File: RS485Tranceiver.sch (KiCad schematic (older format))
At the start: 19 parts, among them J8 Conn_01x02, U9 SN75176AD

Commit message: added filters
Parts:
- removed C30, C31: 470p, Capacitor_SMD:C_0603_1608Metric, symbol AR2ISS:C
- removed C32, C33: 1n, Capacitor_SMD:C_0603_1608Metric, symbol AR2ISS:C
- removed D7: PESD2CAN, Package_TO_SOT_SMD:SOT-23_Handsoldering, symbol Device:D_TVS_x2_AAC
- removed J8: Conn_01x02, Connector_PinHeader_2.54mm:PinHeader_1x02_P2.54mm_Vertical, symbol Connector_Generic:Conn_01x02
- removed L3, L4: 10u, Inductor_SMD:L_0603_1608Metric, symbol Device:L
- removed L5, L6: 74279266, Inductor_SMD:L_0603_1608Metric, symbol Device:L
- removed R16, R17: 221, Resistor_SMD:R_0603_1608Metric, symbol AR2ISS:R
- removed R18: 120, Resistor_SMD:R_0603_1608Metric, symbol AR2ISS:R
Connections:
- net sheet60920273/A_Out: now reaches R20.2, R21.1, U9.6 (A)
- net sheet60920273/B_Out: now reaches R19.2, R20.1, U9.7 (B)

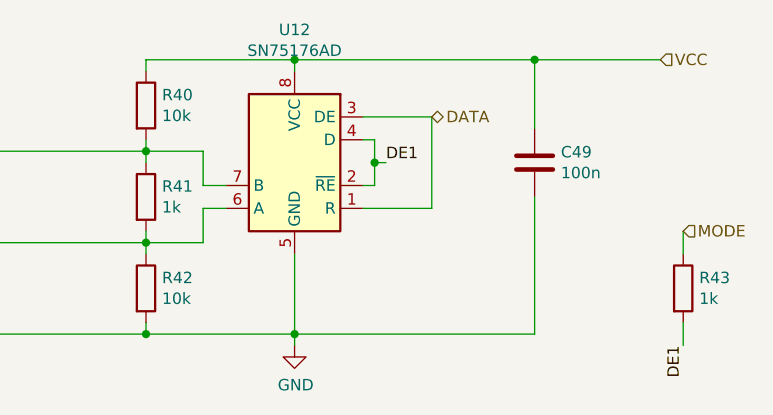
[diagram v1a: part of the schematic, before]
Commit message: updated layout
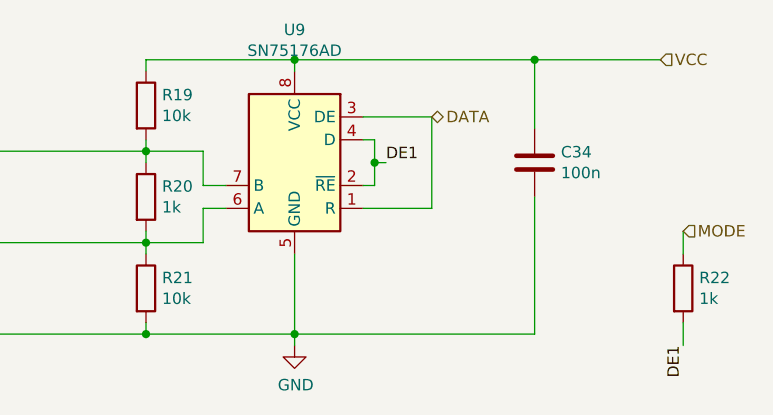
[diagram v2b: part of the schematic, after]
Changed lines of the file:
@@
 $Descr A4 11693 8268
 encoding utf-8
-Sheet 28 31
+Sheet 22 31
 Title ""
 Date ""
@@
 AR Path="/60843FDF/60797D2F/6072BD51" Ref="U10"  Part="1"
 AR Path="/60843FDF/607938CE/6072BD51" Ref="U11"  Part="1"
-F 0 "U12" H 8600 2981 50  0000 C CNN
+F 0 "U9" H 8600 2981 50  0000 C CNN
 F 1 "SN75176AD" H 8600 2890 50  0000 C CNN
 F 2 "Package_SO:SOIC-8_3.9x4.9mm_P1.27mm" H 8600 1900 50  0001 C CNN
@@
 AR Path="/60843FDF/60797D2F/6072BD57" Ref="R28"  Part="1"
 AR Path="/60843FDF/607938CE/6072BD57" Ref="R35"  Part="1"
-F 0 "R42" H 8020 2996 50  0000 L CNN
+F 0 "R21" H 8020 2996 50  0000 L CNN
 F 1 "10k" H 8020 2905 50  0000 L CNN
 F 2 "Resistor_SMD:R_0603_1608Metric" V 7880 2950 50  0001 C CNN
@@
 AR Path="/60843FDF/60797D2F/6072BD5D" Ref="R29"  Part="1"
 AR Path="/60843FDF/607938CE/6072BD5D" Ref="R36"  Part="1"
-F 0 "R43" H 10370 2996 50  0000 L CNN
+F 0 "R22" H 10370 2996 50  0000 L CNN
 F 1 "1k" H 10370 2905 50  0000 L CNN
 F 2 "Resistor_SMD:R_0603_1608Metric" V 10230 2950 50  0001 C CNN
@@
 AR Path="/60843FDF/60797D2F/6072BD63" Ref="R26"  Part="1"
 AR Path="/60843FDF/607938CE/6072BD63" Ref="R33"  Part="1"
-F 0 "R40" H 8020 2196 50  0000 L CNN
+F 0 "R19" H 8020 2196 50  0000 L CNN
 F 1 "10k" H 8020 2105 50  0000 L CNN
 F 2 "Resistor_SMD:R_0603_1608Metric" V 7880 2150 50  0001 C CNN
@@
 AR Path="/60843FDF/60797D2F/6072BD8E" Ref="C39"  Part="1"
 AR Path="/60843FDF/607938CE/6072BD8E" Ref="C44"  Part="1"
-F 0 "C49" H 9765 2446 50  0000 L CNN
+F 0 "C34" H 9765 2446 50  0000 L CNN
 F 1 "100n" H 9765 2355 50  0000 L CNN
 F 2 "Capacitor_SMD:C_0603_1608Metric" H 9688 2250 50  0001 C CNN
@@
 AR Path="/60843FDF/60797D2F/6072BDA0" Ref="R27"  Part="1"
 AR Path="/60843FDF/607938CE/6072BDA0" Ref="R34"  Part="1"
-F 0 "R41" H 8020 2596 50  0000 L CNN
+F 0 "R20" H 8020 2596 50  0000 L CNN
 F 1 "1k" H 8020 2505 50  0000 L CNN
 F 2 "Resistor_SMD:R_0603_1608Metric" V 7880 2550 50  0001 C CNN

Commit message: ready for ordering
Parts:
- R19, R21: value 10k -> NB
- R20: value 1k -> NB
- U9: value SN75176AD -> SP3485; symbol Interface_UART:SN75176AD -> AR2ISS:SP3485
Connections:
- net DATA: now also U9.4 (DI); no longer U9.3 (DE)
- net DE1: now also U9.3 (DE); no longer U9.4 (D)
- net sheet60920273/A_Out: now also R19.2, R20.1; no longer R20.2, R21.1
- net sheet60920273/B_Out: now also R20.2, R21.1; no longer R19.2, R20.1
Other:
- moved on the sheet: U9
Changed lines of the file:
@@
 $EndDescr
 $Comp
-L Interface_UART:SN75176AD U?
+L AR2ISS:SP3485 U?
 U 1 1 6072BD51
-P 8600 2400
+P 8600 2550
 AR Path="/606DDE00/6072BD51" Ref="U?"  Part="1"
 AR Path="/6072BD51" Ref="U?"  Part="1"
@@
 AR Path="/60843FDF/60797D2F/6072BD51" Ref="U10"  Part="1"
 AR Path="/60843FDF/607938CE/6072BD51" Ref="U11"  Part="1"
-F 0 "U9" H 8600 2981 50  0000 C CNN
-F 1 "SN75176AD" H 8600 2890 50  0000 C CNN
-F 2 "Package_SO:SOIC-8_3.9x4.9mm_P1.27mm" H 8600 1900 50  0001 C CNN
-F 3 "http://www.ti.com/lit/ds/symlink/sn75176a.pdf" H 10200 2200 50  0001 C CNN
-	1    8600 2400
+F 0 "U9" H 8600 3131 50  0000 C CNN
+F 1 "SP3485" H 8600 3040 50  0000 C CNN
+F 2 "Package_SO:SOIC-8_3.9x4.9mm_P1.27mm" H 8600 2050 50  0001 C CNN
+F 3 "http://www.ti.com/lit/ds/symlink/sn75176a.pdf" H 10200 2350 50  0001 C CNN
+	1    8600 2550
 	-1   0    0    -1
 $EndComp
@@
 AR Path="/60843FDF/607938CE/6072BD57" Ref="R35"  Part="1"
 F 0 "R21" H 8020 2996 50  0000 L CNN
-F 1 "10k" H 8020 2905 50  0000 L CNN
+F 1 "NB" H 8020 2905 50  0000 L CNN
 F 2 "Resistor_SMD:R_0603_1608Metric" V 7880 2950 50  0001 C CNN
 F 3 "~" H 7950 2950 50  0001 C CNN
@@
 AR Path="/60843FDF/607938CE/6072BD63" Ref="R33"  Part="1"
 F 0 "R19" H 8020 2196 50  0000 L CNN
-F 1 "10k" H 8020 2105 50  0000 L CNN
+F 1 "NB" H 8020 2105 50  0000 L CNN
 F 2 "Resistor_SMD:R_0603_1608Metric" V 7880 2150 50  0001 C CNN
 F 3 "~" H 7950 2150 50  0001 C CNN
@@
 	7950 2350 8200 2350
 Wire Wire Line
-	8200 2350 8200 2500
-Wire Wire Line
-	8200 2500 8300 2500
+	8200 2350 8200 2450
 Connection ~ 7950 2350
 Wire Wire Line
@@
 	7950 2750 8200 2750
 Wire Wire Line
-	8200 2750 8200 2600
-Wire Wire Line
-	8200 2600 8300 2600
+	8200 2750 8200 2650
 Connection ~ 7950 2750
 Wire Wire Line
@@
 Wire Wire Line
 	8600 3150 8600 3200
-Wire Wire Line
-	8600 2800 8600 3150
 Connection ~ 8600 3150
 Wire Wire Line
@@
 	7950 1950 8600 1950
 Wire Wire Line
-	8600 1950 8600 2000
-Wire Wire Line
-	8900 2300 8950 2300
-Wire Wire Line
-	8950 2300 8950 2400
-Wire Wire Line
-	8950 2500 8900 2500
-Wire Wire Line
-	8950 2400 9000 2400
-Connection ~ 8950 2400
-Wire Wire Line
-	8950 2400 8950 2500
-Text Label 9000 2400 0    50   ~ 0
+	9000 2450 9050 2450
+Wire Wire Line
+	9050 2450 9050 2550
+Wire Wire Line
+	9050 2650 9000 2650
+Wire Wire Line
+	9050 2550 9100 2550
+Connection ~ 9050 2550
+Wire Wire Line
+	9050 2550 9050 2650
+Text Label 9100 2550 0    50   ~ 0
 DE1
 Wire Wire Line
-	9200 2200 9200 2600
-Wire Wire Line
-	8900 2200 9200 2200
-Wire Wire Line
-	8900 2600 9200 2600
+	9300 2350 9300 2750
+Wire Wire Line
+	9000 2350 9300 2350
+Wire Wire Line
+	9000 2750 9300 2750
 Text Label 10300 3200 3    50   ~ 0
 DE1
@@
 AR Path="/60843FDF/607938CE/6072BDA0" Ref="R34"  Part="1"
 F 0 "R20" H 8020 2596 50  0000 L CNN
-F 1 "1k" H 8020 2505 50  0000 L CNN
+F 1 "NB" H 8020 2505 50  0000 L CNN
 F 2 "Resistor_SMD:R_0603_1608Metric" V 7880 2550 50  0001 C CNN
 F 3 "~" H 7950 2550 50  0001 C CNN
@@
 	1    0    0    -1
 $EndComp
+Text HLabel 6200 2350 0    50   Input ~ 0
+A_in
 Text HLabel 6200 2750 0    50   Input ~ 0
-A_in
-Text HLabel 6200 2350 0    50   Input ~ 0
 B_in
 Wire Wire Line
@@
 Text HLabel 10200 1950 2    50   Input ~ 0
 VCC
-Text HLabel 9200 2200 2    50   BiDi ~ 0
+Text HLabel 9300 2350 2    50   BiDi ~ 0
 DATA
 $Sheet
@@
 F0 "sheet60920273" 50
 F1 "filter.sch" 50
-F2 "A" I L 6400 2750 50
-F3 "B" I L 6400 2350 50
-F4 "A_Out" I R 7000 2750 50
-F5 "B_Out" I R 7000 2350 50
+F2 "A" I L 6400 2350 50
+F3 "B" I L 6400 2750 50
+F4 "A_Out" I R 7000 2350 50
+F5 "B_Out" I R 7000 2750 50
 F6 "GND" I R 7000 2850 50
 $EndSheet
@@
 	7150 3150 7950 3150
 Connection ~ 7950 3150
+Wire Wire Line
+	8600 2950 8600 3150
+Wire Wire Line
+	8600 1950 8600 2150
 $EndSCHEMATC
